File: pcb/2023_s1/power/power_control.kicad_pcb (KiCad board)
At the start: 2 copper layers, 20 parts, among them J1 Conn_01x05_Male, Q2 TIP122, U1 40106, U3 4N25

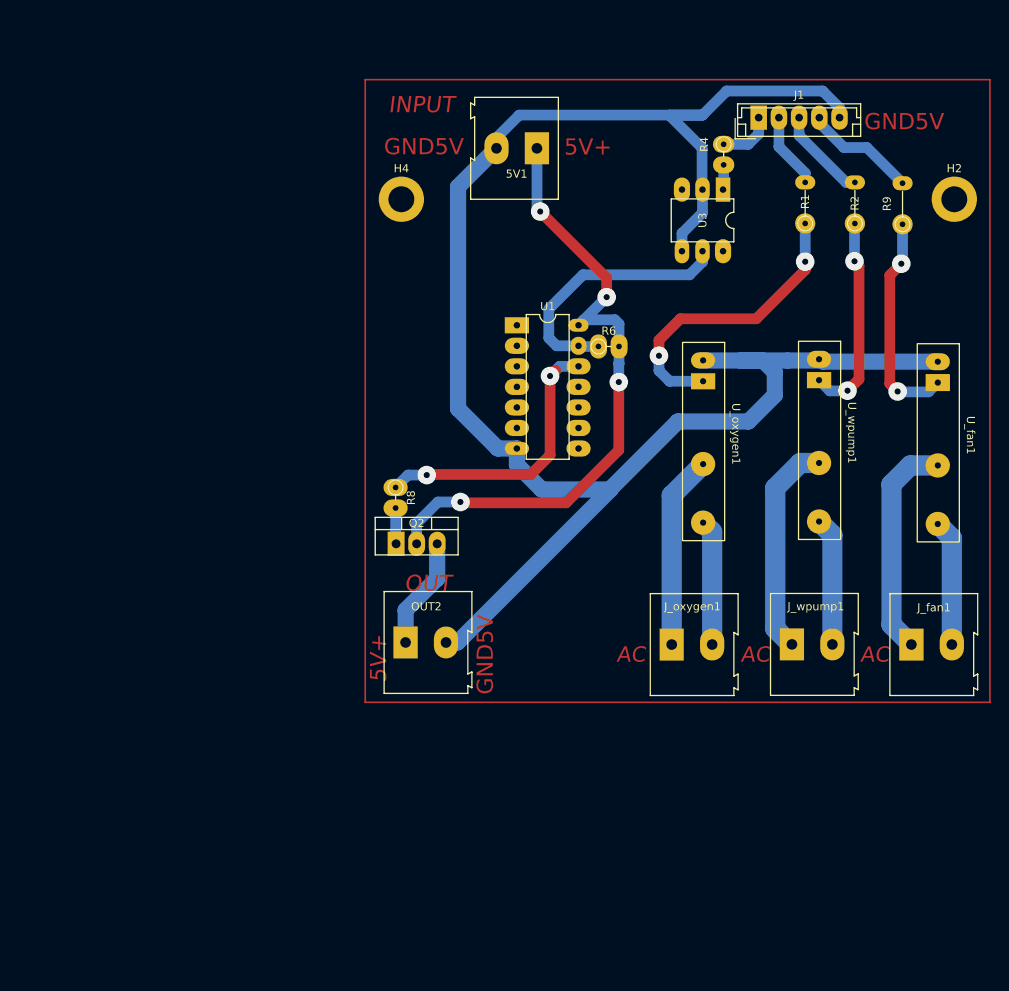
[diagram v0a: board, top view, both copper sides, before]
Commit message: update, changed some terminals to screw terminals for easyer connection
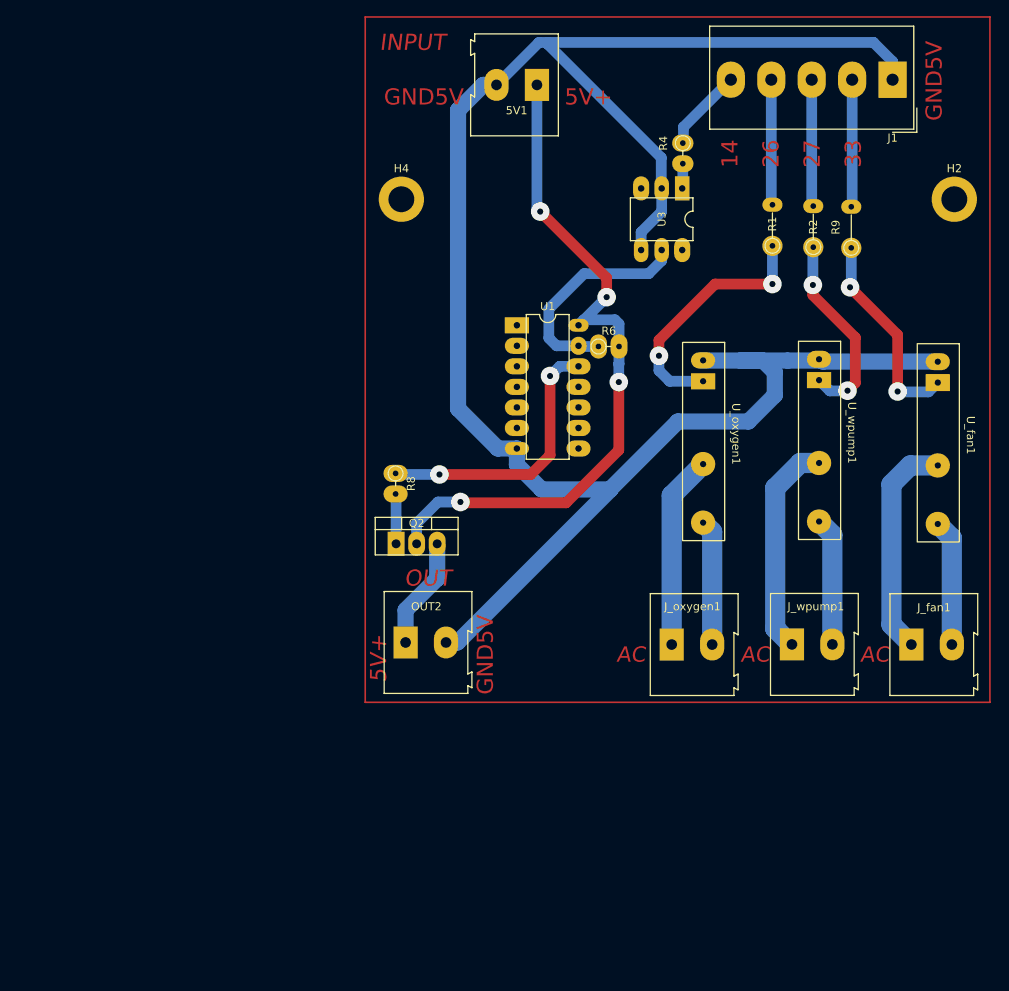
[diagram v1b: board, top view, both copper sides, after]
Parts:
- J1: value Conn_01x05_Male -> Screw_Terminal_01x05; footprint Connector_JST:JST_EH_B5B-EH-A_1x05_P2.50mm_Vertical -> TerminalBlock_Altech:Altech_AK300_1x05_P5.00mm_45-Degree
- moved J1 17.2 mm to (191.9, 38.6), turned to 180 degrees
- moved 5V1 7.84 mm to (147.9, 39.2)
- moved R9 6.98 mm to (186.8, 59.4)
- moved R2 5.92 mm to (182.1, 59.3)
- moved R4 5.05 mm to (165.9, 46.5)
- moved U3 5.05 mm to (165.8, 52.1)
- moved R1 4.90 mm to (177.0, 59.2)
- moved R8 1.74 mm to (130.4, 87.3)
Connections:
- J1 pad 1: D14 -> GND5V
- J1 pad 2: D26 -> D33
- J1 pad 4: D33 -> D26
- J1 pad 5: GND5V -> D14
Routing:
- net GND5V: track 220.8 -> 244.6 mm
- net 5v: track 79.4 -> 87.3 mm
- net D26: track 9.39 -> 15.5 mm
- net Net-(R1-Pad1): track 37.2 -> 31.4 mm
- net Net-(R6-Pad1): track 33.0 -> 28.0 mm
- net D27: track 11.5 -> 15.7 mm
- net D14: track 6.87 -> 10.3 mm
- net Net-(Q2-Pad1): track 4.53 -> 6.27 mm
- net D33: track 14.0 -> 15.8 mm
- net Net-(R9-Pad1): track 27.2 -> 25.5 mm
- net Net-(R8-Pad1): track 35.2 -> 33.6 mm
- net Net-(R2-Pad1): track 25.7 -> 24.3 mm
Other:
- board text added: "14"
- board text added: "26"
- board text added: "27"
- board text added: "33"

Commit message: update, based on experience and practice connecting AC devices proposed a change to the pcb, to make it easier to connect, and more intuitive
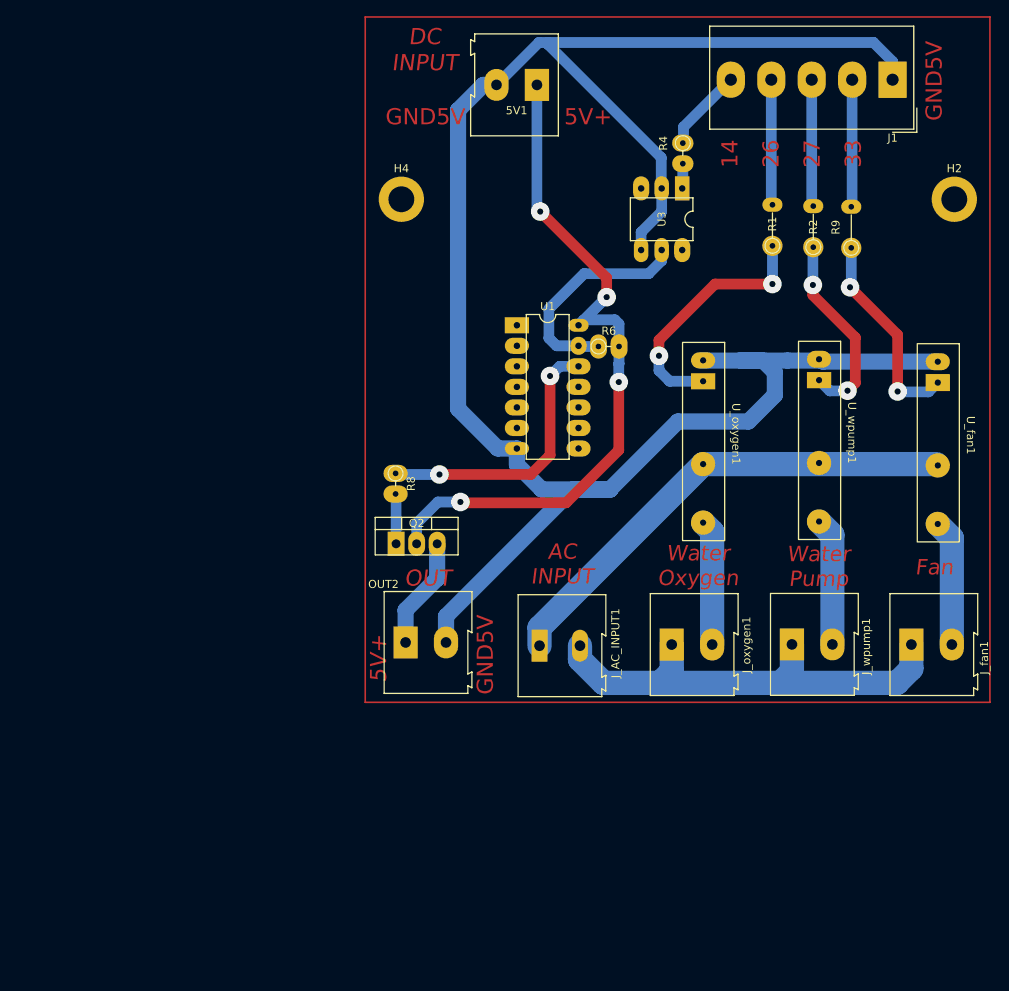
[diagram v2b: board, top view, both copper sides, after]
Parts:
- added J_AC_INPUT1: Screw_Terminal_01x02, TerminalBlock:TerminalBlock_Altech_AK300-2_P5.00mm, F.Cu at (148.2, 108.6)
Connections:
- J_fan1 pad 1: Net-(J_fan1-Pad1) -> AC2
- J_oxygen1 pad 1: Net-(J_oxygen1-Pad1) -> AC2
- J_wpump1 pad 1: Net-(J_wpump1-Pad1) -> AC2
- U_fan1 pad 11: Net-(J_fan1-Pad1) -> AC1
- U_oxygen1 pad 11: Net-(J_oxygen1-Pad1) -> AC1
- U_wpump1 pad 11: Net-(J_wpump1-Pad1) -> AC1
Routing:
- net AC1: track 0.00 -> 59.9 mm
- net AC2: track 0.00 -> 58.4 mm
- net Net-(J_fan1-Pad1): track 27.5 -> 0.00 mm
- net Net-(J_wpump1-Pad1): track 27.0 -> 0.00 mm
- net Net-(J_oxygen1-Pad1): track 23.9 -> 0.00 mm
- net GND5V: track 244.6 -> 246.5 mm
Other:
- board text added: "AC INPUT"
- board text added: "DC INPUT"
- board text added: "Fan"
- board text added: "Water Oxygen"
- board text added: "Water Pump"
- board text removed: "AC"
- board text removed: "INPUT"

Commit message: update, changed pcbs to use mechanic relays instead of the trigger schmith circuit, because of reliability and simpleness of the design
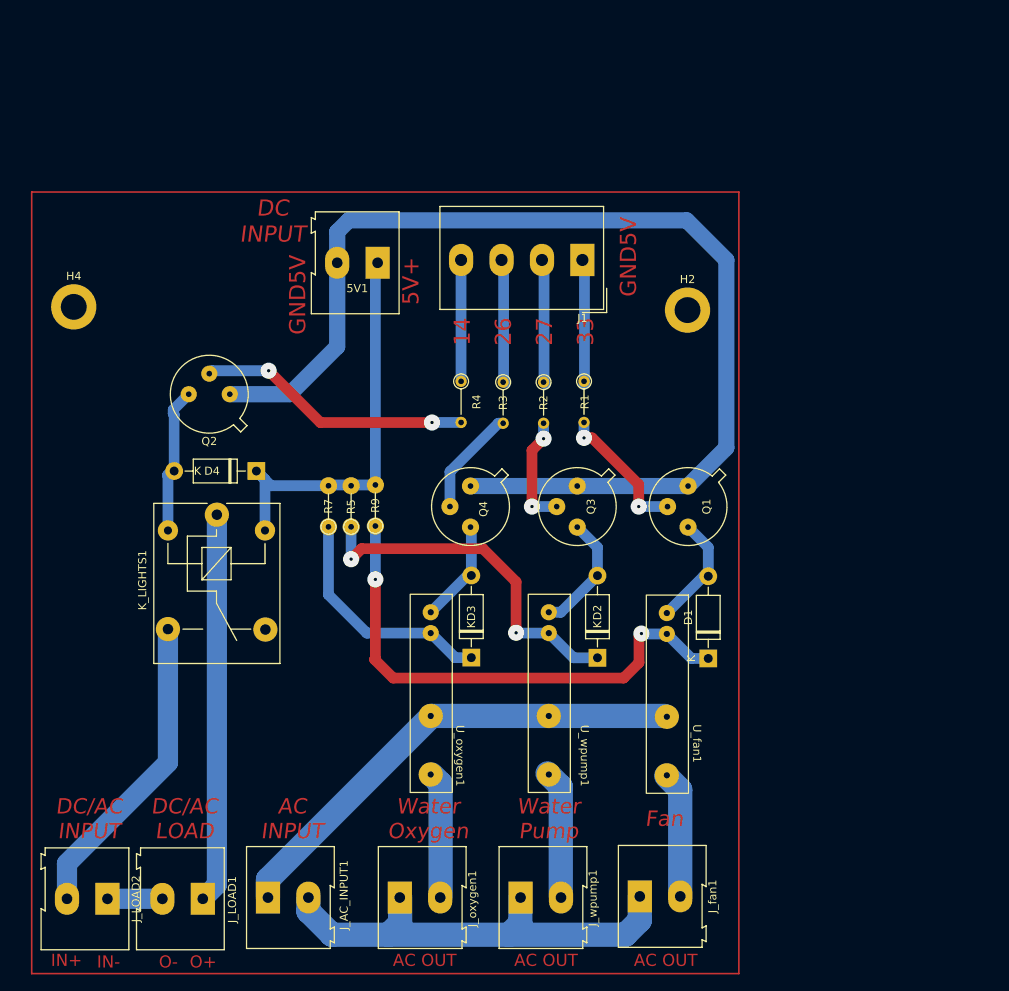
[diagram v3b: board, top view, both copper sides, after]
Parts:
- removed OUT2: Screw_Terminal_01x02, TerminalBlock:TerminalBlock_Altech_AK300-2_P5.00mm
- removed R6: 10k, Resistor_THT:R_Axial_DIN0204_L3.6mm_D1.6mm_P2.54mm_Vertical
- removed R8: 10, Resistor_THT:R_Axial_DIN0204_L3.6mm_D1.6mm_P2.54mm_Vertical
- removed U1: 40106, Package_DIP:DIP-14_W7.62mm
- removed U3: 4N25, Package_DIP:DIP-6_W7.62mm
- added D1: 1N4004, Diode_THT:D_DO-41_SOD81_P10.16mm_Horizontal, F.Cu at (169.1, 110.2)
- added D2: 1N4004, Diode_THT:D_DO-41_SOD81_P10.16mm_Horizontal, F.Cu at (155.4, 110.1)
- added D3: 1N4004, Diode_THT:D_DO-41_SOD81_P10.16mm_Horizontal, F.Cu at (139.8, 110.1)
- added D4: 1N4004, Diode_THT:D_DO-41_SOD81_P10.16mm_Horizontal, F.Cu at (113.2, 87.0)
- added J_LOAD1: Screw_Terminal_01x02, TerminalBlock:TerminalBlock_Altech_AK300-2_P5.00mm, F.Cu at (106.6, 139.9)
- added J_LOAD2: Screw_Terminal_01x02, TerminalBlock:TerminalBlock_Altech_AK300-2_P5.00mm, F.Cu at (94.8, 139.9)
- added K_LIGHTS1: SANYOU_SRD_Form_C, Relay_THT:Relay_SPDT_SANYOU_SRD_Series_Form_C, F.Cu at (108.3, 92.4)
- added Q1: 2N2219, Package_TO_SOT_THT:TO-39-3, F.Cu at (166.6, 88.9)
- added Q3: 2N2219, Package_TO_SOT_THT:TO-39-3, F.Cu at (152.9, 88.9)
- added Q4: 2N2219, Package_TO_SOT_THT:TO-39-3, F.Cu at (139.7, 88.9)
- added R3: 660, Resistor_THT:R_Axial_DIN0204_L3.6mm_D1.6mm_P5.08mm_Vertical, F.Cu at (143.7, 76.0)
- added R5: R, Resistor_THT:R_Axial_DIN0204_L3.6mm_D1.6mm_P5.08mm_Vertical, F.Cu at (124.9, 93.9)
- added R7: R, Resistor_THT:R_Axial_DIN0204_L3.6mm_D1.6mm_P5.08mm_Vertical, F.Cu at (122.1, 93.9)
- J1: value Screw_Terminal_01x05 -> Screw_Terminal_01x04; footprint TerminalBlock_Altech:Altech_AK300_1x05_P5.00mm_45-Degree -> TerminalBlock_Altech:Altech_AK300_1x04_P5.00mm_45-Degree
- Q2: value TIP122 -> 2N2219; footprint Package_TO_SOT_THT:TO-220-3_Vertical -> Package_TO_SOT_THT:TO-39-3
- R1, R2: value R -> 660
- R4: value 100 -> 660; footprint Resistor_THT:R_Axial_DIN0204_L3.6mm_D1.6mm_P2.54mm_Vertical -> Resistor_THT:R_Axial_DIN0204_L3.6mm_D1.6mm_P5.08mm_Vertical
- moved R9 68.2 mm to (127.9, 93.8)
- moved J_oxygen1 45.9 mm to (130.9, 139.7)
- moved J_wpump1 45.9 mm to (145.9, 139.7)
- moved U_oxygen1 45.9 mm to (134.6, 113.5)
- moved J_fan1 45.8 mm to (160.6, 139.6)
- moved J_AC_INPUT1 45.8 mm to (114.6, 139.7)
- moved U_wpump1 45.8 mm to (149.2, 113.5)
- moved U_fan1 45.7 mm to (163.8, 113.6)
- moved J1 44.4 mm to (153.5, 60.9)
- moved H4 42.6 mm to (90.6, 66.7)
- moved R4 40.2 mm to (138.5, 75.9)
- moved R2 37.3 mm to (148.7, 76.0), turned to -90 degrees
- moved H2 35.7 mm to (166.5, 67.1)
- moved 5V1 29.5 mm to (128.2, 61.2)
- moved R1 28.7 mm to (153.7, 75.9), turned to -90 degrees
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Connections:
- J1 pad 1: GND5V -> D33
- J1 pad 2: D33 -> D27
- J1 pad 3: D27 -> D26
- J1 pad 4: D26 -> D14
- Q2 pad 1: Net-(Q2-Pad1) -> GND5V
- Q2 pad 2: 5v -> Net-(Q2-Pad2)
- R1 pad 1: Net-(R1-Pad1) -> D33
- R1 pad 2: D26 -> Net-(Q1-Pad2)
- R2 pad 1: Net-(R2-Pad1) -> D27
- R2 pad 2: D27 -> Net-(Q3-Pad2)
- R4 pad 2: Net-(R4-Pad2) -> Net-(Q2-Pad2)
- R9 pad 2: D33 -> 5v
- U_fan1 pad A2: GND5V -> Net-(D1-Pad2)
- U_oxygen1 pad A1: Net-(R1-Pad1) -> Net-(D3-Pad1)
- U_oxygen1 pad A2: GND5V -> Net-(D3-Pad2)
- U_wpump1 pad A1: Net-(R2-Pad1) -> Net-(D2-Pad1)
- U_wpump1 pad A2: GND5V -> Net-(D2-Pad2)
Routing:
- net GND5V: track 246.5 -> 137.5 mm
- net LOAD IN: track 0.00 -> 48.2 mm
- net Net-(D2-Pad1): track 0.00 -> 44.3 mm, vias 0 -> 2
- net Net-(D1-Pad1): track 25.5 -> 64.2 mm
- net Normally O: track 0.00 -> 38.5 mm
- net 5v: track 87.3 -> 50.9 mm, vias 4 -> 0
- net Net-(Q2-Pad2): track 0.00 -> 33.9 mm, vias 0 -> 2
- net Net-(R8-Pad1): track 33.6 -> 0.00 mm, vias 2 -> 0
- net Net-(R1-Pad1): track 31.4 -> 0.00 mm, vias 2 -> 0
- net Net-(D3-Pad1): track 0.00 -> 29.5 mm
- net Net-(R6-Pad1): track 28.0 -> 0.00 mm
- net Net-(R2-Pad1): track 24.3 -> 0.00 mm, vias 2 -> 0
- net Net-(Q1-Pad2): track 0.00 -> 17.4 mm, vias 0 -> 2
- net Net-(D2-Pad2): track 0.00 -> 15.0 mm
- net Net-(D1-Pad2): track 0.00 -> 14.1 mm
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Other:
- board text added: "AC OUT"
- board text added: "DC/AC INPUT"
- board text added: "DC/AC LOAD"
- board text added: "IN+"
- board text added: "IN-"
- board text added: "O+"
- board text added: "O-"
- board text removed: "OUT"

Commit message: update
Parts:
- added R6: R, Resistor_THT:R_Axial_DIN0204_L3.6mm_D1.6mm_P5.08mm_Vertical, B.Cu at (137.7, 93.9)
- 5V1, D1, D2, D3, D4, H2, H4, J1, J_AC_INPUT1, J_LOAD1, J_LOAD2, J_fan1, J_oxygen1, J_wpump1, K_LIGHTS1, Q1, Q2, Q3, Q4, R1, R2, R3, R4, R5, R7, R9, U_fan1, U_oxygen1, U_wpump1: moved to B.Cu
- moved D1 81.7 mm to (87.4, 110.2)
- moved Q1 76.7 mm to (89.9, 88.9)
- moved H2 76.6 mm to (89.9, 67.1), turned to 180 degrees
- moved H4 75.2 mm to (165.8, 66.7), turned to 180 degrees
- moved U_fan1 71.2 mm to (92.6, 113.6)
- moved J_LOAD2 66.9 mm to (161.7, 139.9), turned to 0 degrees
- moved J_fan1 64.8 mm to (95.8, 139.6), turned to 180 degrees
- moved D2 54.3 mm to (101.1, 110.1)
- moved R1 51.0 mm to (102.7, 75.9)
- moved J1 50.6 mm to (102.9, 60.9), turned to 0 degrees
- moved Q3 49.3 mm to (103.6, 88.9)
- moved J_LOAD1 43.3 mm to (149.9, 139.9), turned to 0 degrees
- moved U_wpump1 42.0 mm to (107.2, 113.5)
- moved R2 41.0 mm to (107.7, 76.0)
- moved K_LIGHTS1 39.8 mm to (148.1, 92.4)
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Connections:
- D4 pad 1: 5v -> Net-(D4-Pad1)
- K_LIGHTS1 pad 5: 5v -> Net-(D4-Pad1)
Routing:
- net 5v: track 50.9 -> 36.8 mm
- net Net-(D4-Pad1): track 0.00 -> 12.7 mm
- net Net-(D2-Pad1): track 44.3 -> 43.2 mm
- net Net-(Q3-Pad2): track 14.0 -> 14.8 mm
- net Net-(Q1-Pad2): track 17.4 -> 16.8 mm
